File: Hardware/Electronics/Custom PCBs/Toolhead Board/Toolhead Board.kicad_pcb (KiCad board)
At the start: 2 copper layers, 65 x 65 mm, 0 parts

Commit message: Get basic Toolhead Board outline
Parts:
- added C1: 1u/100V, Capacitor_SMD:C_0805_2012Metric_Pad1.18x1.45mm_HandSolder, F.Cu at (170.8, 72.3)
- added C10: 100n, Capacitor_SMD:C_0603_1608Metric_Pad1.08x0.95mm_HandSolder, F.Cu at (209.4, 31.1)
- added C11: 100n, Capacitor_SMD:C_0603_1608Metric_Pad1.08x0.95mm_HandSolder, F.Cu at (209.4, 33.6)
- added C12: 100n, Capacitor_SMD:C_0603_1608Metric_Pad1.08x0.95mm_HandSolder, F.Cu at (209.4, 36.1)
- added C13: 100n, Capacitor_SMD:C_0603_1608Metric_Pad1.08x0.95mm_HandSolder, F.Cu at (213.8, 18.5)
- added C14: 100n, Capacitor_SMD:C_0603_1608Metric_Pad1.08x0.95mm_HandSolder, F.Cu at (213.8, 21.0)
- added C15: 100n, Capacitor_SMD:C_0603_1608Metric_Pad1.08x0.95mm_HandSolder, F.Cu at (213.8, 23.6)
- added C16: 100n, Capacitor_SMD:C_0603_1608Metric_Pad1.08x0.95mm_HandSolder, F.Cu at (213.8, 26.1)
- added C17: 22p, Capacitor_SMD:C_0603_1608Metric_Pad1.08x0.95mm_HandSolder, F.Cu at (213.8, 28.6)
- added C18: 22p, Capacitor_SMD:C_0603_1608Metric_Pad1.08x0.95mm_HandSolder, F.Cu at (213.8, 31.1)
- added C19: 1u, Capacitor_SMD:C_0603_1608Metric_Pad1.08x0.95mm_HandSolder, F.Cu at (139.5, 60.2)
- added C2: 1u, Capacitor_SMD:C_0603_1608Metric_Pad1.08x0.95mm_HandSolder, F.Cu at (171.5, 60.2)
- added C20: 100n, Capacitor_SMD:C_0603_1608Metric_Pad1.08x0.95mm_HandSolder, F.Cu at (139.5, 62.7)
- added C21: 47p, Capacitor_SMD:C_0603_1608Metric_Pad1.08x0.95mm_HandSolder, F.Cu at (139.5, 65.2)
- added C22: 47p, Capacitor_SMD:C_0603_1608Metric_Pad1.08x0.95mm_HandSolder, F.Cu at (139.5, 67.7)
- added C23: 100n, Capacitor_SMD:C_0603_1608Metric_Pad1.08x0.95mm_HandSolder, F.Cu at (139.5, 70.2)
- added C24: 100n, Capacitor_SMD:C_0603_1608Metric_Pad1.08x0.95mm_HandSolder, F.Cu at (208.7, 54.4)
- added C25: 100n, Capacitor_SMD:C_0603_1608Metric_Pad1.08x0.95mm_HandSolder, F.Cu at (208.7, 56.9)
- added C26: 100u, Capacitor_THT:CP_Radial_D8.0mm_P3.50mm, F.Cu at (183.6, 91.0)
- added C27: 22n, Capacitor_SMD:C_0603_1608Metric_Pad1.08x0.95mm_HandSolder, F.Cu at (208.7, 59.4)
- added C28: 100n, Capacitor_SMD:C_0603_1608Metric_Pad1.08x0.95mm_HandSolder, F.Cu at (208.7, 61.9)
- added C29: 4.7u, Capacitor_SMD:C_0603_1608Metric_Pad1.08x0.95mm_HandSolder, F.Cu at (208.7, 64.4)
- added C3: 1u, Capacitor_SMD:C_0603_1608Metric_Pad1.08x0.95mm_HandSolder, F.Cu at (171.5, 62.7)
- added C30: 100n, Capacitor_SMD:C_0603_1608Metric_Pad1.08x0.95mm_HandSolder, F.Cu at (208.7, 66.9)
- added C31: 10uF, Capacitor_SMD:C_0805_2012Metric, F.Cu at (168.9, 38.3)
- added C32: 0.1uF, Capacitor_SMD:C_0603_1608Metric_Pad1.08x0.95mm_HandSolder, F.Cu at (165.6, 18.5)
- added C33: 10uF, Capacitor_SMD:C_0805_2012Metric, F.Cu at (168.9, 41.4)
- added C34: 0.1uF, Capacitor_SMD:C_0603_1608Metric_Pad1.08x0.95mm_HandSolder, F.Cu at (165.6, 21.0)
- added C35: 0.1uF, Capacitor_SMD:C_0603_1608Metric_Pad1.08x0.95mm_HandSolder, F.Cu at (165.6, 23.6)
- added C36: 0.1uF, Capacitor_SMD:C_0603_1608Metric_Pad1.08x0.95mm_HandSolder, F.Cu at (165.6, 26.1)
- added C37: 10uF, Capacitor_SMD:C_0805_2012Metric, F.Cu at (168.9, 44.4)
- added C38: 0.1uF, Capacitor_SMD:C_0603_1608Metric, F.Cu at (164.7, 38.1)
- added C39: 10uF, Capacitor_SMD:C_0805_2012Metric, F.Cu at (168.9, 47.4)
- added C4: 1u, Capacitor_SMD:C_0603_1608Metric_Pad1.08x0.95mm_HandSolder, F.Cu at (171.5, 65.2)
- added C40: 0.1uF, Capacitor_SMD:C_0603_1608Metric, F.Cu at (164.7, 40.6)
- added C41: 0.1uF, Capacitor_SMD:C_0603_1608Metric, F.Cu at (164.7, 43.1)
- added C42: 0.1uF, Capacitor_SMD:C_0603_1608Metric, F.Cu at (164.7, 45.6)
- added C43: 10uF, Capacitor_SMD:C_0805_2012Metric, F.Cu at (168.9, 50.4)
- added C44: 0.1uF, Capacitor_SMD:C_0603_1608Metric, F.Cu at (164.7, 48.1)
- added C45: 10uF, Capacitor_SMD:C_0805_2012Metric, F.Cu at (168.9, 53.4)
- added C46: 0.1uF, Capacitor_SMD:C_0603_1608Metric, F.Cu at (164.7, 50.6)
- added C47: 0.1uF, Capacitor_SMD:C_0603_1608Metric, F.Cu at (164.7, 53.1)
- added C48: 0.1uF, Capacitor_SMD:C_0603_1608Metric, F.Cu at (164.7, 55.7)
- added C49: 100n, Capacitor_SMD:C_0603_1608Metric_Pad1.08x0.95mm_HandSolder, F.Cu at (208.7, 78.9)
- added C5: 1u, Capacitor_SMD:C_0603_1608Metric_Pad1.08x0.95mm_HandSolder, F.Cu at (209.4, 18.5)
- added C50: 10u, Capacitor_SMD:C_0805_2012Metric_Pad1.18x1.45mm_HandSolder, F.Cu at (198.3, 54.6)
- added C51: 10u, Capacitor_SMD:C_0805_2012Metric_Pad1.18x1.45mm_HandSolder, F.Cu at (198.3, 57.6)
- added C52: 10u, Capacitor_SMD:C_0805_2012Metric_Pad1.18x1.45mm_HandSolder, F.Cu at (198.3, 60.6)
- added C53: 10u, Capacitor_SMD:C_0805_2012Metric_Pad1.18x1.45mm_HandSolder, F.Cu at (198.3, 63.6)
- added C54: 10u, Capacitor_SMD:C_0805_2012Metric_Pad1.18x1.45mm_HandSolder, F.Cu at (198.3, 66.6)
- added C6: 1u, Capacitor_SMD:C_0603_1608Metric_Pad1.08x0.95mm_HandSolder, F.Cu at (209.4, 21.0)
- added C7: 100n, Capacitor_SMD:C_0603_1608Metric_Pad1.08x0.95mm_HandSolder, F.Cu at (209.4, 23.6)
- added C8: 100n, Capacitor_SMD:C_0603_1608Metric_Pad1.08x0.95mm_HandSolder, F.Cu at (209.4, 26.1)
- added C9: 100n, Capacitor_SMD:C_0603_1608Metric_Pad1.08x0.95mm_HandSolder, F.Cu at (209.4, 28.6)
- added CR1: PESD1CAN_215, Package_TO_SOT_SMD:SOT-23, F.Cu at (152.6, 76.9)
- added D1: LED, LED_SMD:LED_1206_3216Metric_Pad1.42x1.75mm_HandSolder, F.Cu at (202.1, 48.1)
- added H1: MountingHole, MountingHole:MountingHole_3.2mm_M3_DIN965_Pad, F.Cu at (87.5, 75.0)
- added H2: MountingHole, MountingHole:MountingHole_3.2mm_M3_DIN965_Pad, F.Cu at (68.8, 85.8)
- added H3: MountingHole, MountingHole:MountingHole_3.2mm_M3_DIN965_Pad, F.Cu at (68.8, 64.2)
- added H4: MountingHole, MountingHole:MountingHole_3.2mm_M3_DIN965_Pad, F.Cu at (154.8, 87.8)
- added H5: MountingHole, MountingHole:MountingHole_3.2mm_M3_DIN965_Pad, F.Cu at (154.8, 95.8)
- added H6: MountingHole, MountingHole:MountingHole_3.2mm_M3_DIN965_Pad, F.Cu at (154.8, 103.0)
- added H7: MountingHole, MountingHole:MountingHole_3.2mm_M3_DIN965_Pad, F.Cu at (162.0, 88.7)
- added H8: MountingHole, MountingHole:MountingHole_3.2mm_M3_DIN965_Pad, F.Cu at (162.0, 95.8)
- added H9: MountingHole, MountingHole:MountingHole_3.2mm_M3_DIN965_Pad, F.Cu at (162.0, 103.0)
- added J1: USB C Receptacle, Connector_USB:USB_C_Receptacle_GCT_USB4105-xx-A_16P_TopMnt_Horizontal, B.Cu at (41.0, 75.0)
- added J10: Conn_01x02, Connector_JST:JST_XH_B2B-XH-AM_1x02_P2.50mm_Vertical, B.Cu at (50.8, 80.5)
- added J11: Conn_01x02, Connector_JST:JST_XH_B2B-XH-AM_1x02_P2.50mm_Vertical, B.Cu at (50.8, 72.0)
- added J12: 120TR, Connector_PinHeader_2.54mm:PinHeader_1x02_P2.54mm_Vertical, B.Cu at (51.2, 85.3)
- added J2: Conn_02x08_Odd_Even, Connector_PinSocket_2.54mm:PinSocket_2x08_P2.54mm_Vertical, F.Cu at (59.5, 83.9)
- added J3: Conn_02x08_Odd_Even, Connector_PinSocket_2.54mm:PinSocket_2x08_P2.54mm_Vertical, F.Cu at (75.1, 57.1)
- added J4: Conn_02x08_Odd_Even, Connector_PinSocket_2.54mm:PinSocket_2x08_P2.54mm_Vertical, F.Cu at (90.4, 84.0)
- added J5: Conn_02x04_Odd_Even, Connector_PinSocket_2.54mm:PinSocket_2x04_P2.54mm_Vertical, F.Cu at (70.0, 71.2)
- added J6: Conn_02x04_Odd_Even, Connector_PinSocket_2.54mm:PinSocket_2x04_P2.54mm_Vertical, F.Cu at (76.3, 71.2)
- added JP1: SolderJumper_2_Open, Jumper:SolderJumper-2_P1.3mm_Open_RoundedPad1.0x1.5mm, F.Cu at (213.1, 71.7)
- added JP2: SolderJumper_3_Bridged123, Jumper:SolderJumper-3_P1.3mm_Open_RoundedPad1.0x1.5mm, F.Cu at (213.7, 79.5)
- added JP3: SolderJumper_2_Open, Jumper:SolderJumper-2_P1.3mm_Open_RoundedPad1.0x1.5mm, F.Cu at (213.1, 87.7)
- added JP4: SolderJumper_2_Open, Jumper:SolderJumper-2_P1.3mm_Open_RoundedPad1.0x1.5mm, F.Cu at (180.6, 54.9)
- added JP5: SolderJumper_2_Open, Jumper:SolderJumper-2_P1.3mm_Open_RoundedPad1.0x1.5mm, F.Cu at (180.6, 58.4)
- added JP6: SolderJumper_2_Open, Jumper:SolderJumper-2_P1.3mm_Open_RoundedPad1.0x1.5mm, F.Cu at (180.6, 62.0)
- added JP7: SolderJumper_2_Open, Jumper:SolderJumper-2_P1.3mm_Open_RoundedPad1.0x1.5mm, F.Cu at (180.6, 65.5)
- added JP8: SolderJumper_2_Open, Jumper:SolderJumper-2_P1.3mm_Open_RoundedPad1.0x1.5mm, F.Cu at (180.6, 69.1)
- added JP9: SolderJumper_2_Open, Jumper:SolderJumper-2_P1.3mm_Open_RoundedPad1.0x1.5mm, F.Cu at (180.6, 72.6)
- added L1: 3.3uH, Inductor_SMD:L_0805_2012Metric, F.Cu at (139.6, 49.8)
- added L2: 3.3uH, Inductor_SMD:L_0805_2012Metric, F.Cu at (139.6, 52.6)
- added L3: 3.3uH, Inductor_SMD:L_0805_2012Metric, F.Cu at (139.6, 55.3)
- added NT1: NetTie_2, NetTie:NetTie-2_SMD_Pad0.5mm, F.Cu at (143.1, 49.2)
- added Q1: MMBT4403, Package_TO_SOT_SMD:SOT-23, F.Cu at (173.6, 39.2)
- added Q2: MMBT4403, Package_TO_SOT_SMD:SOT-23, F.Cu at (173.6, 43.9)
- added Q3: MMBT4403, Package_TO_SOT_SMD:SOT-23, F.Cu at (173.6, 48.5)
- added R1: 10k, Resistor_SMD:R_0603_1608Metric_Pad0.98x0.95mm_HandSolder, F.Cu at (213.8, 33.6)
- added R10: NC, Resistor_SMD:R_0603_1608Metric_Pad0.98x0.95mm_HandSolder, F.Cu at (139.5, 72.7)
- added R11: 120, Resistor_SMD:R_0603_1608Metric_Pad0.98x0.95mm_HandSolder, F.Cu at (139.5, 75.2)
- added R12: 0R11, Resistor_SMD:R_0603_1608Metric_Pad0.98x0.95mm_HandSolder, F.Cu at (208.7, 69.4)
- added R13: 0R11, Resistor_SMD:R_0603_1608Metric_Pad0.98x0.95mm_HandSolder, F.Cu at (208.7, 71.9)
- added R14: 100, Resistor_SMD:R_0603_1608Metric_Pad0.98x0.95mm_HandSolder, F.Cu at (208.7, 74.4)
- added R15: 330, Resistor_SMD:R_2512_6332Metric, F.Cu at (105.7, 75.0)
- added R16: 330, Resistor_SMD:R_2512_6332Metric, B.Cu at (105.7, 75.0)
- added R17: 330, Resistor_SMD:R_2512_6332Metric, F.Cu at (59.7, 48.5)
- added R18: 330, Resistor_SMD:R_2512_6332Metric, B.Cu at (59.7, 48.5)
- added R19: 330, Resistor_SMD:R_2512_6332Metric, F.Cu at (59.7, 101.5)
- added R2: 10k, Resistor_SMD:R_0603_1608Metric_Pad0.98x0.95mm_HandSolder, F.Cu at (213.8, 36.1)
- added R20: 330, Resistor_SMD:R_2512_6332Metric, B.Cu at (59.7, 101.5)
- added R21: 10k, Resistor_SMD:R_0603_1608Metric_Pad0.98x0.95mm_HandSolder, F.Cu at (165.6, 28.6)
- added R22: 330, Resistor_SMD:R_2512_6332Metric, F.Cu at (98.0, 75.0)
- added R23: 330, Resistor_SMD:R_2512_6332Metric, B.Cu at (98.0, 75.0)
- added R24: 330, Resistor_SMD:R_2512_6332Metric, F.Cu at (63.5, 55.1)
- added R25: 330, Resistor_SMD:R_2512_6332Metric, B.Cu at (63.5, 55.1)
- added R26: 330, Resistor_SMD:R_2512_6332Metric, F.Cu at (63.5, 94.9)
- added R27: 330, Resistor_SMD:R_2512_6332Metric, B.Cu at (63.5, 94.9)
- added R28: 8.2k, Resistor_SMD:R_0603_1608Metric_Pad0.98x0.95mm_HandSolder, F.Cu at (165.6, 31.1)
- added R29: 100, Resistor_SMD:R_0603_1608Metric_Pad0.98x0.95mm_HandSolder, F.Cu at (169.9, 18.5)
- added R3: 10k, Resistor_SMD:R_0603_1608Metric_Pad0.98x0.95mm_HandSolder, F.Cu at (218.1, 18.5)
- added R30: 100, Resistor_SMD:R_0603_1608Metric_Pad0.98x0.95mm_HandSolder, F.Cu at (169.9, 21.0)
- added R31: 10k, Resistor_SMD:R_0603_1608Metric_Pad0.98x0.95mm_HandSolder, F.Cu at (169.9, 23.6)
- added R32: 8.2k, Resistor_SMD:R_0603_1608Metric_Pad0.98x0.95mm_HandSolder, F.Cu at (169.9, 26.1)
- added R33: 100, Resistor_SMD:R_0603_1608Metric_Pad0.98x0.95mm_HandSolder, F.Cu at (169.9, 28.6)
- added R34: 100, Resistor_SMD:R_0603_1608Metric_Pad0.98x0.95mm_HandSolder, F.Cu at (169.9, 31.1)
- added R35: 10k, Resistor_SMD:R_0603_1608Metric_Pad0.98x0.95mm_HandSolder, F.Cu at (174.3, 18.5)
- added R36: 8.2k, Resistor_SMD:R_0603_1608Metric_Pad0.98x0.95mm_HandSolder, F.Cu at (174.3, 21.0)
- added R37: 100, Resistor_SMD:R_0603_1608Metric_Pad0.98x0.95mm_HandSolder, F.Cu at (174.3, 23.6)
- added R38: 100, Resistor_SMD:R_0603_1608Metric_Pad0.98x0.95mm_HandSolder, F.Cu at (174.3, 26.1)
- added R39: 2.2k, Resistor_SMD:R_0603_1608Metric_Pad0.98x0.95mm_HandSolder, F.Cu at (208.7, 81.5)
- added R4: 1k, Resistor_SMD:R_0603_1608Metric_Pad0.98x0.95mm_HandSolder, F.Cu at (218.1, 21.0)
- added R40: 2.2k, Resistor_SMD:R_0603_1608Metric_Pad0.98x0.95mm_HandSolder, F.Cu at (208.7, 84.0)
- added R41: 10k, Resistor_SMD:R_0603_1608Metric_Pad0.98x0.95mm_HandSolder, F.Cu at (208.7, 86.5)
- added R42: 100, Resistor_SMD:R_0603_1608Metric_Pad0.98x0.95mm_HandSolder, F.Cu at (185.0, 54.4)
- added R43: 100, Resistor_SMD:R_0603_1608Metric_Pad0.98x0.95mm_HandSolder, F.Cu at (185.0, 56.9)
- added R44: 10k, Resistor_SMD:R_0603_1608Metric_Pad0.98x0.95mm_HandSolder, F.Cu at (185.0, 59.4)
- added R45: 100, Resistor_SMD:R_0603_1608Metric_Pad0.98x0.95mm_HandSolder, F.Cu at (185.0, 61.9)
- added R46: 10k, Resistor_SMD:R_0603_1608Metric_Pad0.98x0.95mm_HandSolder, F.Cu at (185.0, 64.4)
- added R47: 100, Resistor_SMD:R_0603_1608Metric_Pad0.98x0.95mm_HandSolder, F.Cu at (185.0, 66.9)
- added R48: 10k, Resistor_SMD:R_0603_1608Metric_Pad0.98x0.95mm_HandSolder, F.Cu at (185.0, 69.4)
- added R49: 10k, Resistor_SMD:R_0603_1608Metric_Pad0.98x0.95mm_HandSolder, F.Cu at (185.0, 71.9)
- added R5: 1k, Resistor_SMD:R_0603_1608Metric_Pad0.98x0.95mm_HandSolder, F.Cu at (218.1, 23.6)
- added R50: 10k, Resistor_SMD:R_0603_1608Metric_Pad0.98x0.95mm_HandSolder, F.Cu at (189.3, 54.4)
- added R51: 10k, Resistor_SMD:R_0603_1608Metric_Pad0.98x0.95mm_HandSolder, F.Cu at (189.3, 56.9)
- added R52: 10k, Resistor_SMD:R_0603_1608Metric_Pad0.98x0.95mm_HandSolder, F.Cu at (189.3, 59.4)
- added R53: 10k, Resistor_SMD:R_0603_1608Metric_Pad0.98x0.95mm_HandSolder, F.Cu at (189.3, 61.9)
- added R54: 10k, Resistor_SMD:R_0603_1608Metric_Pad0.98x0.95mm_HandSolder, F.Cu at (189.3, 64.4)
- added R55: 10k, Resistor_SMD:R_0603_1608Metric_Pad0.98x0.95mm_HandSolder, F.Cu at (189.3, 66.9)
- added R56: 10k, Resistor_SMD:R_0603_1608Metric_Pad0.98x0.95mm_HandSolder, F.Cu at (189.3, 69.4)
- added R57: 2.2k, Resistor_SMD:R_0603_1608Metric_Pad0.98x0.95mm_HandSolder, F.Cu at (189.3, 71.9)
- added R58: 2.2k, Resistor_SMD:R_0603_1608Metric_Pad0.98x0.95mm_HandSolder, F.Cu at (193.7, 54.4)
- added R59: 2.2k, Resistor_SMD:R_0603_1608Metric_Pad0.98x0.95mm_HandSolder, F.Cu at (193.7, 56.9)
- added R6: 5.1k, Resistor_SMD:R_0603_1608Metric_Pad0.98x0.95mm_HandSolder, F.Cu at (218.1, 26.1)
- added R60: 2.2k, Resistor_SMD:R_0603_1608Metric_Pad0.98x0.95mm_HandSolder, F.Cu at (193.7, 59.4)
- added R7: 5.1k, Resistor_SMD:R_0603_1608Metric_Pad0.98x0.95mm_HandSolder, F.Cu at (218.1, 28.6)
- added R8: 27.4, Resistor_SMD:R_0603_1608Metric_Pad0.98x0.95mm_HandSolder, F.Cu at (218.1, 31.1)
- added R9: 27.4, Resistor_SMD:R_0603_1608Metric_Pad0.98x0.95mm_HandSolder, F.Cu at (218.1, 33.6)
- added RV1: CG0603MLC-3.3LE, Resistor_SMD:R_0603_1608Metric_Pad0.98x0.95mm_HandSolder, F.Cu at (193.7, 61.9)
- added RV2: CG0603MLC-3.3LE, Resistor_SMD:R_0603_1608Metric_Pad0.98x0.95mm_HandSolder, F.Cu at (193.7, 64.4)
- added RV3: CG0603MLC-3.3LE, Resistor_SMD:R_0603_1608Metric_Pad0.98x0.95mm_HandSolder, F.Cu at (193.7, 66.9)
- added RV4: CG0603MLC-3.3LE, Resistor_SMD:R_0603_1608Metric_Pad0.98x0.95mm_HandSolder, F.Cu at (193.7, 69.4)
- added SW1: BOOT, Button_Switch_SMD:SW_SPST_B3U-1000P, F.Cu at (190.7, 41.9)
- added SW2: RESET, Button_Switch_SMD:SW_SPST_B3U-1000P, F.Cu at (190.7, 46.2)
- added TP1: TestPoint, TestPoint:TestPoint_Pad_D1.5mm, F.Cu at (159.6, 72.6)
- added TP2: TestPoint, TestPoint:TestPoint_Pad_D1.5mm, F.Cu at (159.6, 76.2)
- added TP3: TestPoint, TestPoint:TestPoint_Pad_D1.5mm, F.Cu at (163.1, 72.6)
- added TP4: TestPoint, TestPoint:TestPoint_Pad_D1.5mm, F.Cu at (163.1, 76.2)
- added TP5: TestPoint, TestPoint:TestPoint_Pad_D1.5mm, F.Cu at (166.7, 72.6)
- added TP6: TestPoint, TestPoint:TestPoint_Pad_1.5x1.5mm, F.Cu at (166.7, 76.2)
- added U1: LF15_TO220, Package_TO_SOT_THT:TO-220-3_Vertical, F.Cu at (132.2, 93.6)
- added U10: BMI270, Package_LGA:Bosch_LGA-14_3x2.5mm_P0.5mm, F.Cu at (213.4, 83.8)
- added U11: G20N06D52, lib:WDFN-8-1EP_6x5mm_P1.27mm_EP3.4x4mm_No_Center_Pad, F.Cu at (200.4, 71.5)
- added U12: G20N06D52, lib:WDFN-8-1EP_6x5mm_P1.27mm_EP3.4x4mm_No_Center_Pad, F.Cu at (200.4, 78.1)
- added U13: PCA9685BS, Package_DFN_QFN:QFN-28-1EP_6x6mm_P0.65mm_EP4.25x4.25mm, F.Cu at (186.9, 77.3)
- added U2: LF15_TO220, Package_TO_SOT_THT:TO-220-3_Vertical, F.Cu at (161.0, 68.8)
- added U3: RP2040, Package_DFN_QFN:QFN-56-1EP_7x7mm_P0.4mm_EP3.2x3.2mm, F.Cu at (183.1, 44.3)
- added U4: W25Q128JVS, Package_SO:SOIC-8_5.23x5.23mm_P1.27mm, F.Cu at (198.8, 43.1)
- added U5: SN65HVD1050D, Package_SO:SOIC-8_3.9x4.9mm_P1.27mm, F.Cu at (145.9, 77.9)
- added U6: TMC2209-LA, Package_DFN_QFN:QFN-28-1EP_5x5mm_P0.5mm_EP3.75x3.75mm_ThermalVias, F.Cu at (214.5, 66.3)
- added U7: HX711, Package_SO:SOIC-16_3.9x9.9mm_P1.27mm, F.Cu at (141.6, 42.7)
- added U8: HX711, Package_SO:SOIC-16_3.9x9.9mm_P1.27mm, F.Cu at (150.0, 42.7)
- added U9: HX711, Package_SO:SOIC-16_3.9x9.9mm_P1.27mm, F.Cu at (158.5, 42.7)
- added Y1: 12MHz/12pF/50Ω/20ppm, Oscillator:Oscillator_SMD_SeikoEpson_SG210-4Pin_2.5x2.0mm_HandSoldering, F.Cu at (196.3, 48.8)
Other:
- board size 65 x 65 mm -> 75 x 75 mm
- copper layers 2 -> 6

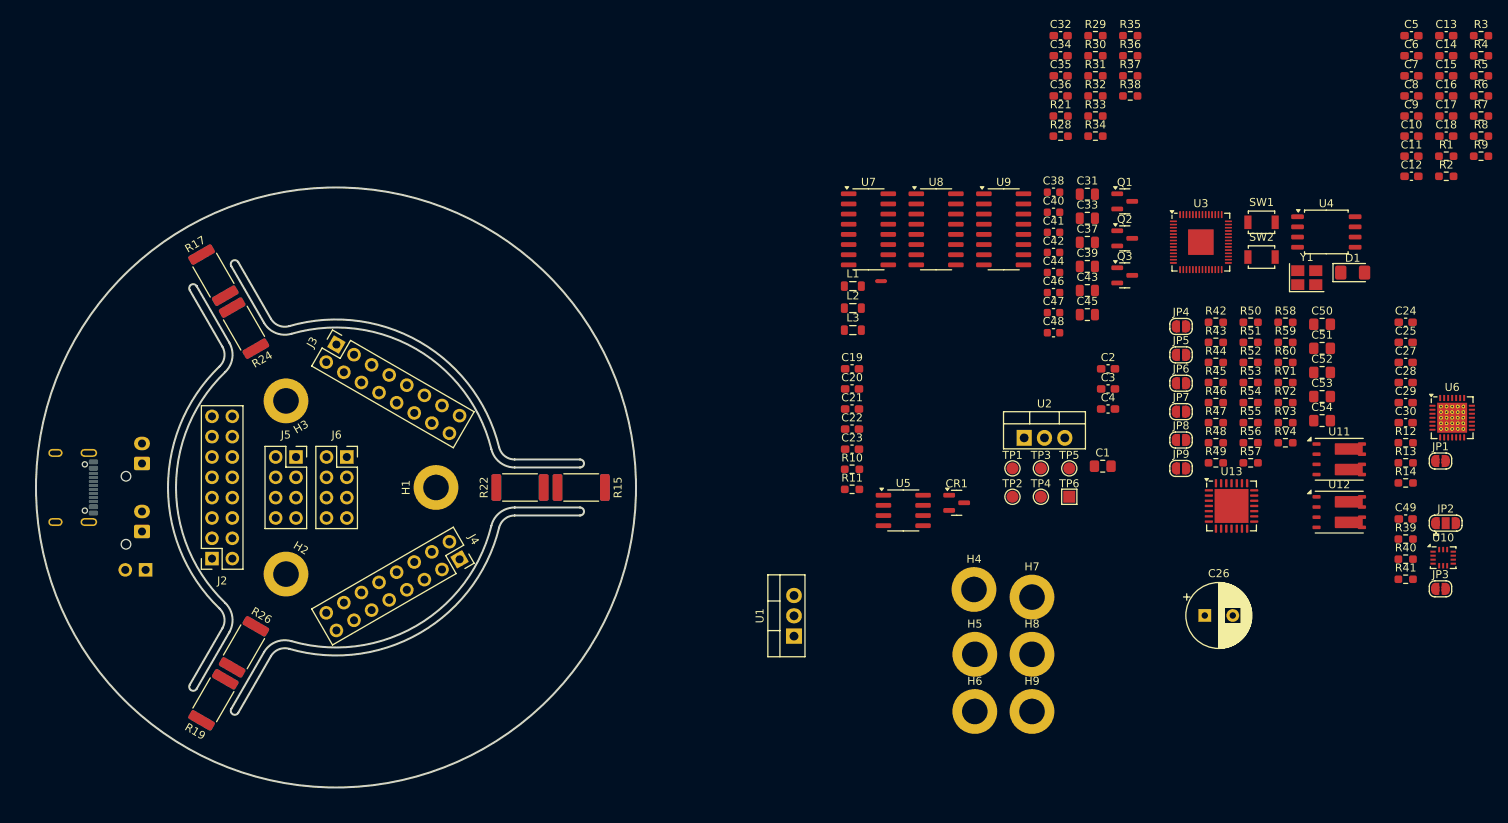
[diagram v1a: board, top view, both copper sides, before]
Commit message: Begin layout and routing of toolhead board
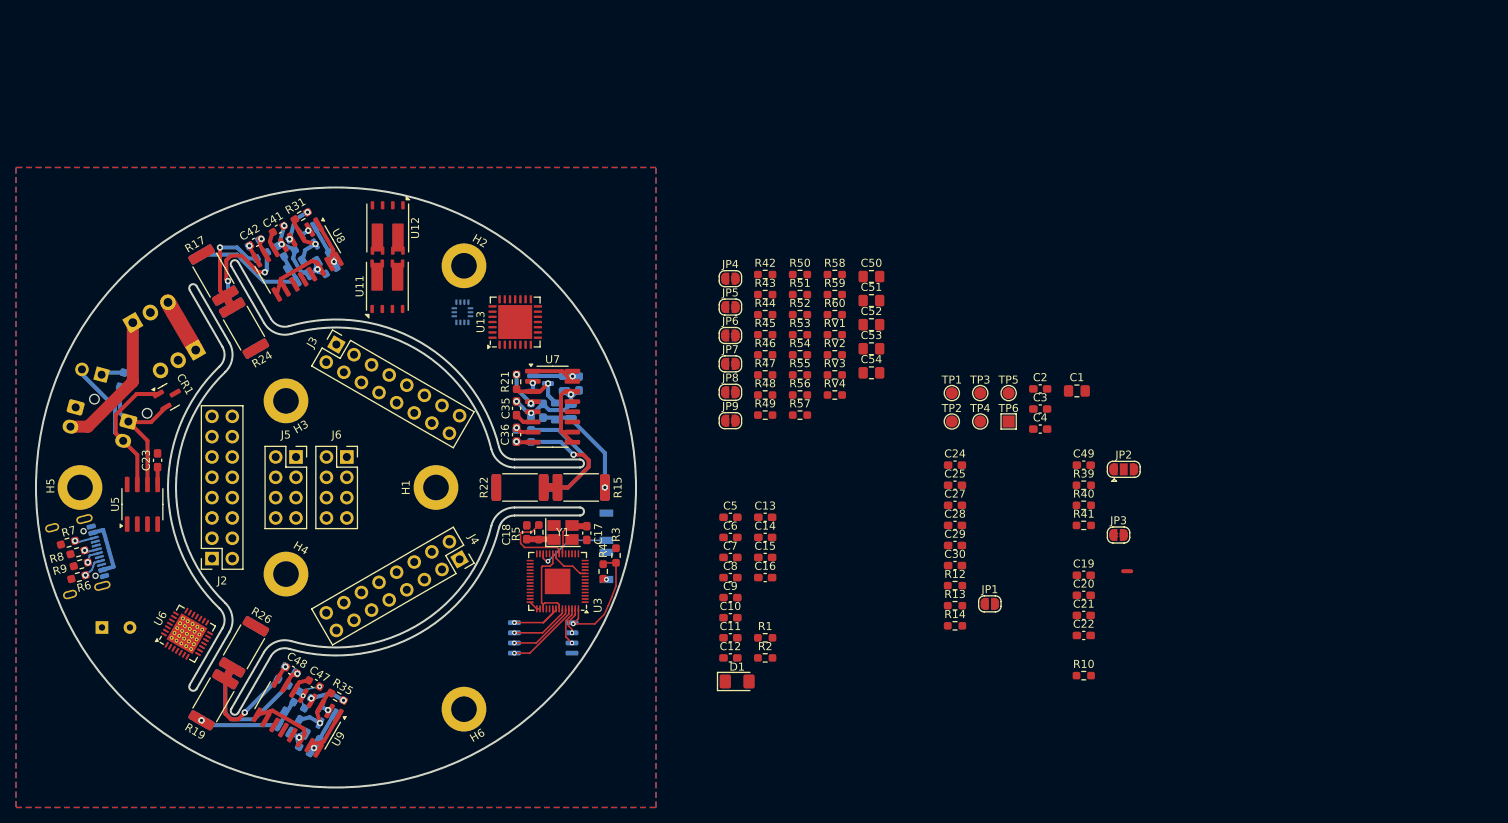
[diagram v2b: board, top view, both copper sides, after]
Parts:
- removed H7, H8, H9: MountingHole, MountingHole:MountingHole_3.2mm_M3_DIN965_Pad
- C26, C31, C32, C33, C34, C37, C38, C39, C40, C43, C44, C45, C46, L1, L2, L3, Q1, Q2, Q3, R11, R28, R29, R30, R32, R33, R34, R36, R37, R38, SW1, SW2, U1, U10, U2, U4: moved to B.Cu
- moved R6 185.4 mm to (42.8, 86.2), turned to -165 degrees
- moved R7 184.5 mm to (41.5, 81.9), turned to -165 degrees
- moved R8 183.0 mm to (42.7, 83.1), turned to -165 degrees
- moved R9 182.3 mm to (43.1, 84.6), turned to 15 degrees
- moved U6 160.4 mm to (56.4, 93.3), turned to 60 degrees
- moved C26 137.9 mm to (45.7, 92.5)
- moved R5 130.9 mm to (100.3, 80.6), turned to 90 degrees
- moved R36 130.5 mm to (71.1, 100.9), turned to 150 degrees
- moved R37 129.1 mm to (69.5, 98.9), turned to -120 degrees
- moved R35 129.0 mm to (75.2, 101.2), turned to -30 degrees
- moved R38 128.3 mm to (68.2, 98.2), turned to 60 degrees
- moved R4 127.3 mm to (108.4, 85.5), turned to 90 degrees
- moved U10 126.4 mm to (90.8, 53.1), turned to 90 degrees
- moved R3 126.1 mm to (110.0, 83.5), turned to 90 degrees
- moved C18 125.1 mm to (98.8, 80.6), turned to -90 degrees
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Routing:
- net GNDA: track 0.00 -> 64.2 mm, vias 0 -> 9
- net +3V3: track 0.00 -> 35.8 mm, vias 0 -> 3
- net /CAN IO/CAN_H: track 0.00 -> 27.3 mm
- net /CAN IO/CAN_L: track 0.00 -> 19.2 mm
- net V_MOT: track 0.00 -> 17.5 mm
- net /Load Cell Amplifiers/STRAIN2_E+: track 0.00 -> 16.8 mm
- net /Load Cell Amplifiers/STRAIN1_S-: track 0.00 -> 16.3 mm
- net /Load Cell Amplifiers/STRAIN3_S-: track 0.00 -> 15.9 mm
- net /Load Cell Amplifiers/STRAIN1_S+: track 0.00 -> 15.7 mm, vias 0 -> 1
- net /Load Cell Amplifiers/STRAIN3_S+: track 0.00 -> 15.1 mm, vias 0 -> 1
- net /Microcontroller/QSPI_SS: track 0.00 -> 14.9 mm, vias 0 -> 1
- net /Load Cell Amplifiers/STRAIN2_S-: track 0.00 -> 14.9 mm, vias 0 -> 2
- net +3.3V: track 0.00 -> 14.7 mm, vias 0 -> 1
- net /Load Cell Amplifiers/STRAIN1_E+: track 0.00 -> 13.9 mm, vias 0 -> 1
- net /Load Cell Amplifiers/STRAIN3_E+: track 0.00 -> 13.3 mm, vias 0 -> 1
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- added copper zone on B.Cu, net GND
- added copper zone on F.Cu, net GND
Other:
- board text added: "BOOT"
- board text added: "CAN"
- board text added: "PWR"
- board text added: "RST"

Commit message: Update toolhead
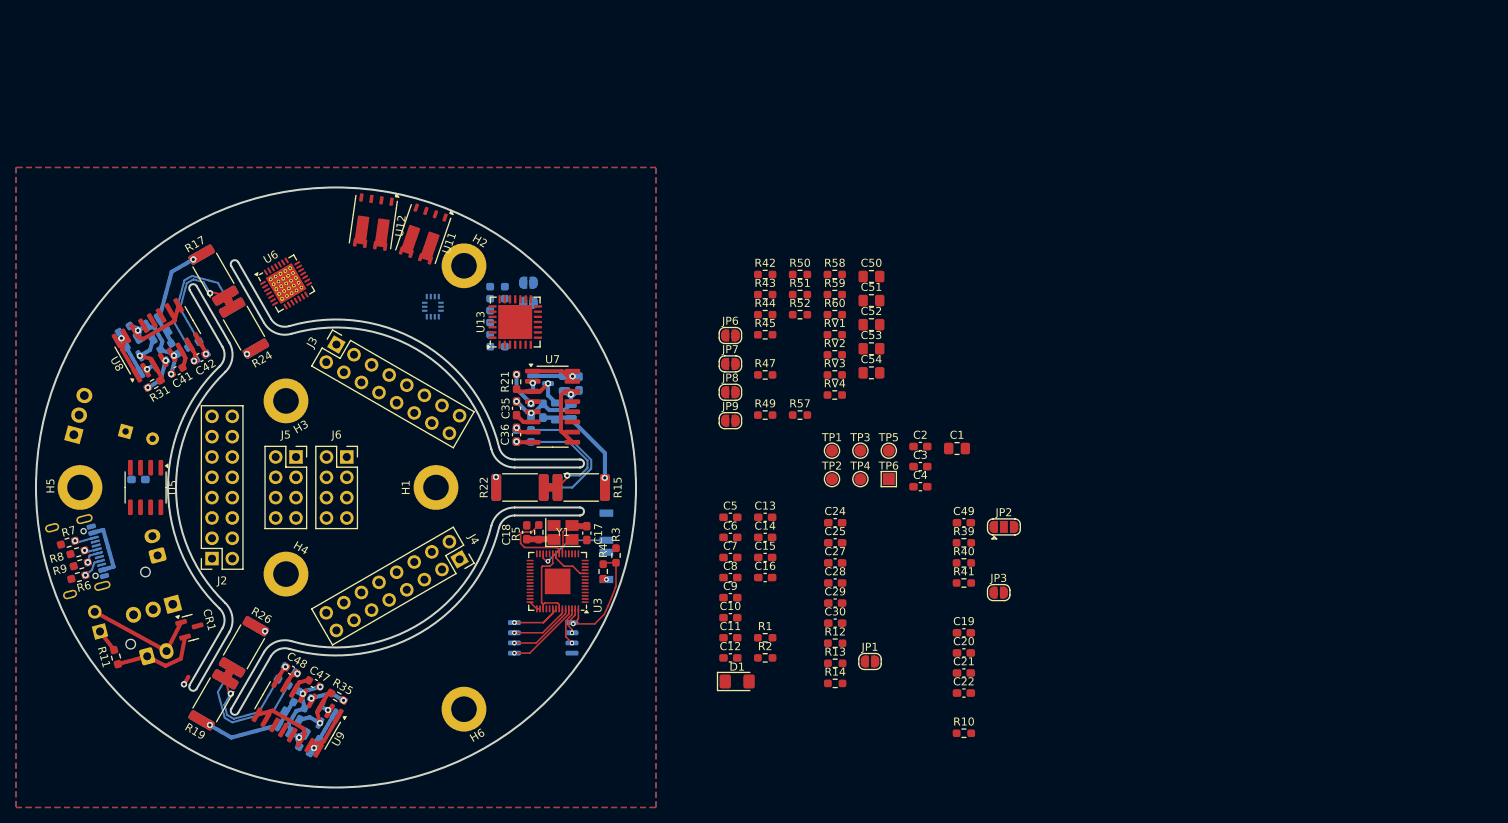
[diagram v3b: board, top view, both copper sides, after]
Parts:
- C23, JP4, JP5, R46, R48, R53, R54, R55, R56: moved to B.Cu
- R11: moved to F.Cu
- moved NT1 118.4 mm to (56.3, 99.1), turned to 60 degrees
- moved U6 45.5 mm to (68.8, 49.5), turned to 30 degrees
- moved R56 38.3 mm to (95.2, 57.4), turned to 180 degrees
- moved R55 38.1 mm to (95.2, 55.9), turned to 180 degrees
- moved R54 38.0 mm to (95.2, 54.4), turned to 180 degrees
- moved R53 37.9 mm to (95.2, 52.9), turned to 180 degrees
- moved R48 35.6 mm to (95.2, 51.4), turned to 180 degrees
- moved R11 34.7 mm to (47.5, 96.2), turned to -75 degrees
- moved R46 34.5 mm to (95.2, 49.9), turned to 180 degrees
- moved J12 32.1 mm to (45.5, 93.0), turned to 15 degrees
- moved U2 31.9 mm to (54.6, 89.6), turned to -165 degrees
- moved J10 29.4 mm to (51.4, 96.1), turned to 15 degrees
- moved CR1 29.0 mm to (56.8, 92.5), turned to 15 degrees
- moved R31 27.9 mm to (52.3, 62.1), turned to -150 degrees
- moved C38 26.8 mm to (48.6, 55.2), turned to 30 degrees
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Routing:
- net GNDA: track 64.2 -> 189.3 mm, vias 9 -> 13
- net +5V: track 6.90 -> 66.9 mm
- net V_MOT: track 17.5 -> 44.6 mm
- net /CAN IO/CAN_H: track 27.3 -> 14.3 mm
- net /CAN IO/CAN_L: track 19.2 -> 11.2 mm
- net /Load Cell Amplifiers/STRAIN2_S+: track 13.1 -> 17.3 mm
- net /Load Cell Amplifiers/STRAIN2_S-: track 14.9 -> 18.8 mm, vias 2 -> 0
- net /Load Cell Amplifiers/STRAIN2_E+: track 16.8 -> 13.9 mm, vias 0 -> 1
- net /Load Cell Amplifiers/STRAIN3_S-: track 15.9 -> 18.8 mm
- net /Load Cell Amplifiers/STRAIN3_S+: track 15.1 -> 17.3 mm
- net Net-(U5-VREF): track 2.16 -> 0.00 mm
- net /Load Cell Amplifiers/STRAIN1_S-: track 16.3 -> 17.1 mm
- net /Load Cell Amplifiers/STRAIN3_E+: track 13.3 -> 13.9 mm
